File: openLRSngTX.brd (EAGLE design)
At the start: 50 x 40 mm, 33 parts, among them IC1 RFM23BPSMD, J1 AVR_SPI_PRG_6PTH, Q1 MMBT2222, U1 ATMEGA328P, X1 BU-SMA-V, Y1 16MHz

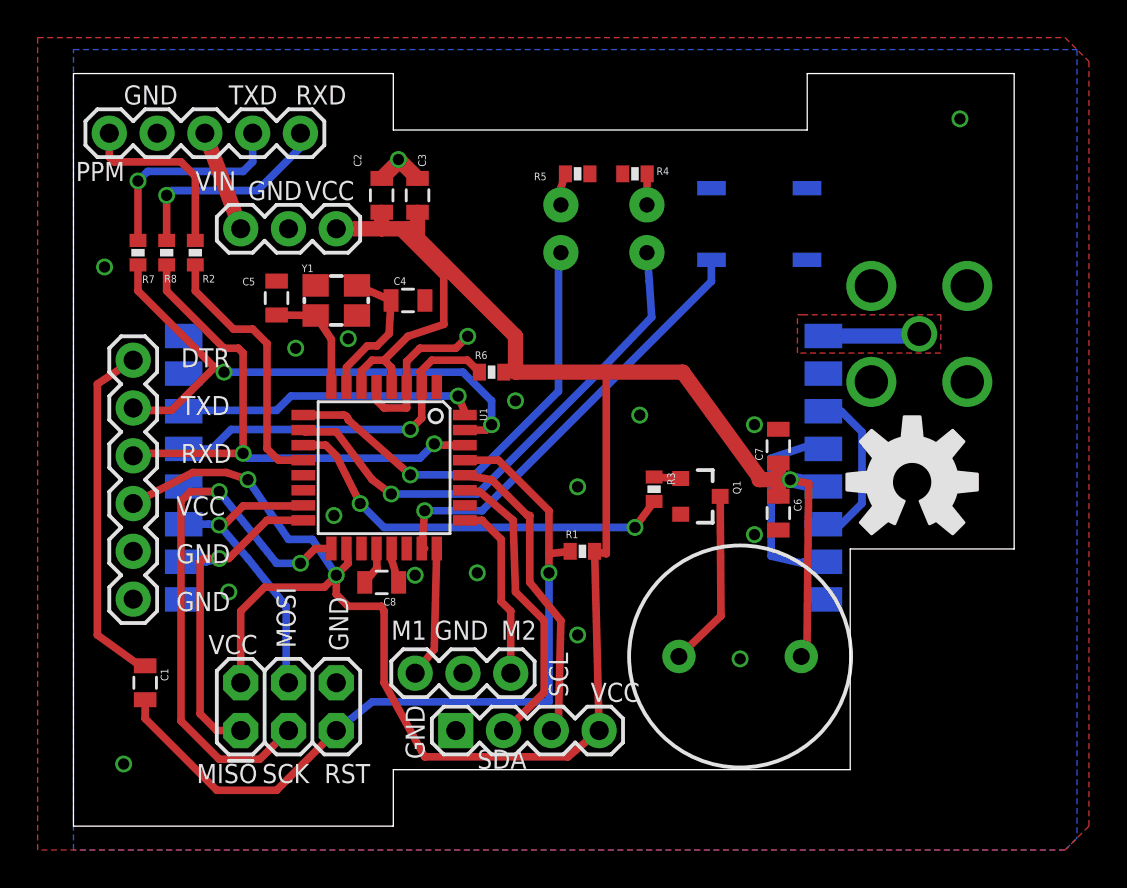
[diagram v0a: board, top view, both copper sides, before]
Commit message: Fix connector towards transmitter (it was wrong way around!). Minor clearance cleanups.
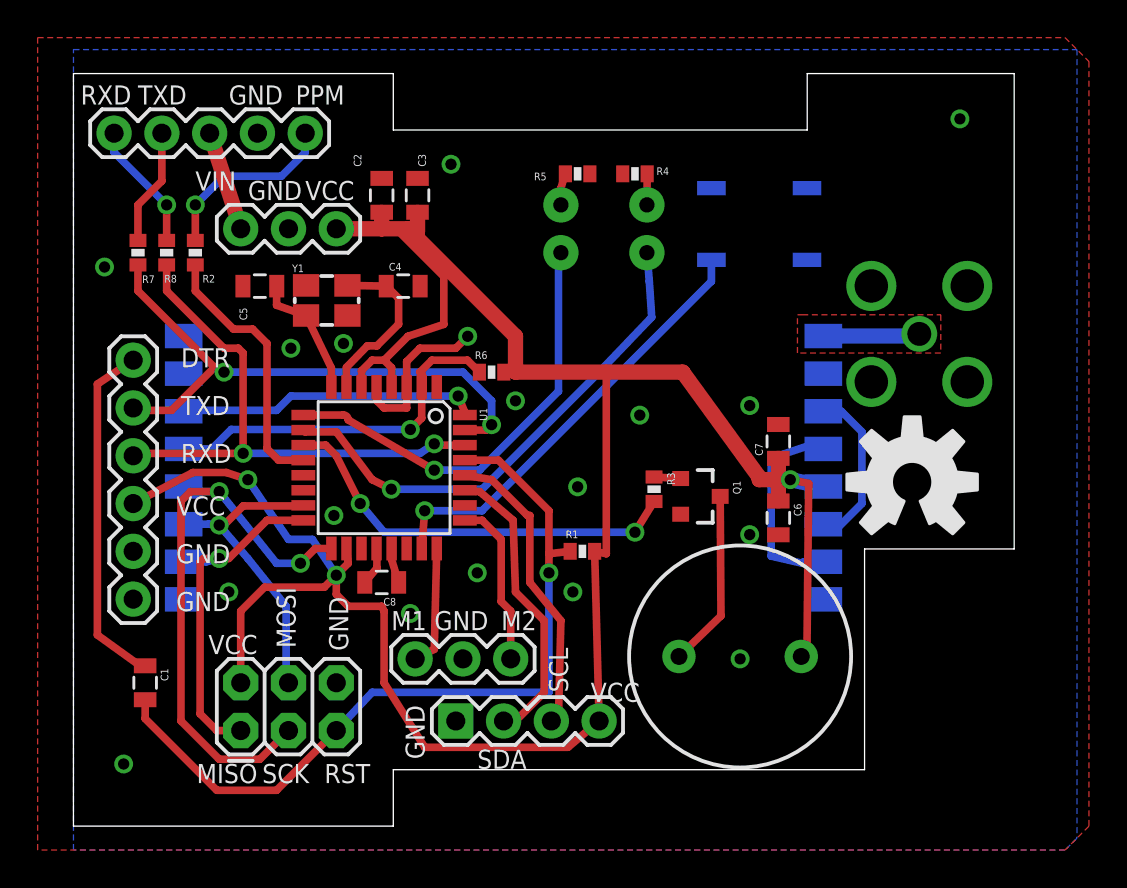
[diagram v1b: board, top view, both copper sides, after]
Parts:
- moved JP1 10.4 mm to (11.7, 36.8), turned to 180 degrees
- moved C5 1.09 mm to (9.27, 28.7), turned to 180 degrees
- moved C4 0.80 mm to (16.9, 28.7)
- moved JP5 0.76 mm to (17.5, 8.89)
- moved Y1 0.51 mm to (12.8, 27.9)
- moved JP3 0.51 mm to (19.7, 5.59)
- moved C6 0.25 mm to (36.8, 16.4)
- moved C7 0.25 mm to (36.8, 20.4)
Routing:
- net N$17: track 11.2 -> 6.23 mm, vias 1 -> 0
- net N$20: track 11.3 -> 6.86 mm
- net GND: track 13.4 -> 10.6 mm
- net N$11: track 7.81 -> 9.14 mm
- net N$19: track 9.67 -> 8.91 mm
- net N$3: track 9.68 -> 9.91 mm, vias 0 -> 1
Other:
- outline, holes or cut-outs redrawn

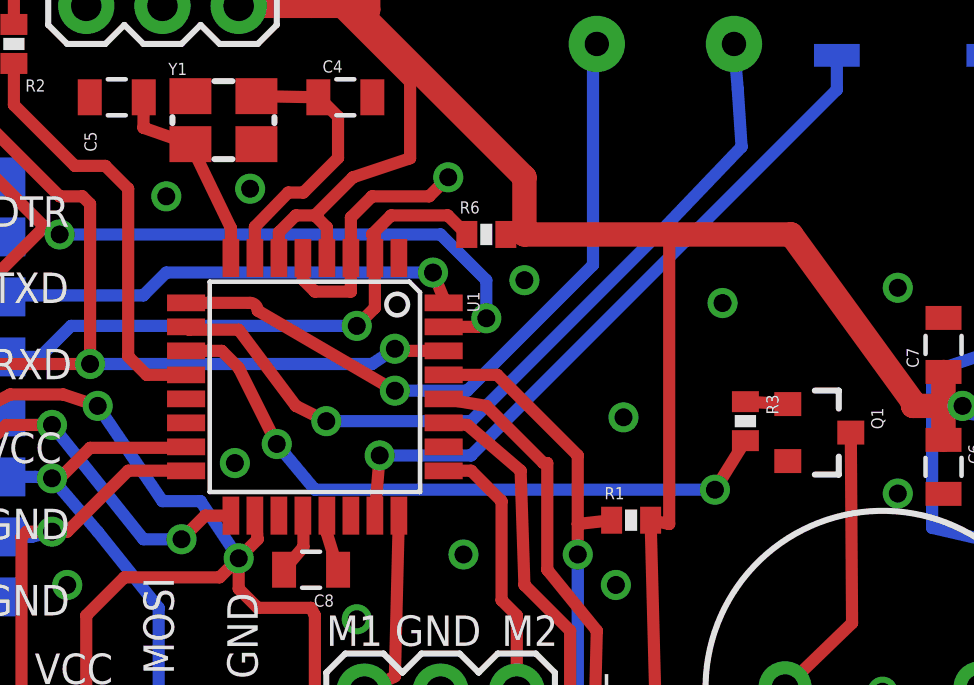
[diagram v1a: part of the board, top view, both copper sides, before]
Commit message: Fix buzzer to correct pin.
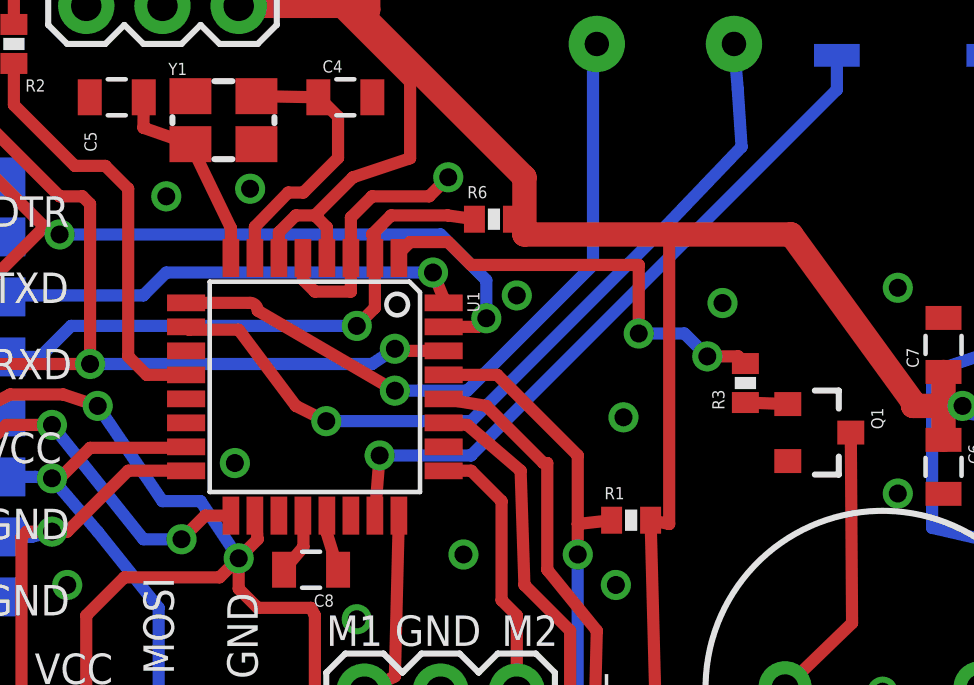
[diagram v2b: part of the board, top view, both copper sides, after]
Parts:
- moved R3 1.27 mm to (30.2, 19.2), turned to 90 degrees
- moved R6 0.57 mm to (21.8, 24.6)
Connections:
- net N$4: now also U1.1; no longer U1.11
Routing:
- net N$4: track 22.1 -> 14.9 mm
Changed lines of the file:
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@@
 <attribute name="VALUE" x="6.2865" y="28.321" size="0.4064" layer="27"/>
 </element>
-<element name="R3" library="SparkFun-Resistors" package="0402-RES" value="1k" x="30.226" y="17.907" rot="R270"/>
+<element name="R3" library="SparkFun-Resistors" package="0402-RES" value="1k" x="30.226" y="19.177" rot="R90"/>
 <element name="R4" library="SparkFun-Resistors" package="0402-RES" value="220R" x="29.21" y="34.671" smashed="yes">
 <attribute name="NAME" x="30.353" y="34.6075" size="0.4064" layer="25"/>
@@
 <element name="C6" library="SparkFun-Capacitors" package="0805" value="1uF" x="36.83" y="16.383" rot="R270"/>
 <element name="C7" library="SparkFun-Capacitors" package="0805" value="100n" x="36.83" y="20.447" rot="R90"/>
-<element name="R6" library="SparkFun-Resistors" package="0402-RES" value="1k" x="21.59" y="24.13"/>
+<element name="R6" library="SparkFun-Resistors" package="0402-RES" value="1k" x="21.844" y="24.638"/>
 <element name="C8" library="SparkFun-Capacitors" package="0805" value="100n" x="15.748" y="12.954" rot="R180"/>
 <element name="S1" library="SparkFun-Electromechanical" package="TACTILE_SWITCH_SMD" value="SWITCH-MOMENTARY-2SMD" x="35.814" y="32.004" smashed="yes" rot="MR180">
@@
 <via x="26.162" y="18.034" extent="1-16" drill="0.6"/>
 <via x="1.016" y="29.718" extent="1-16" drill="0.6"/>
-<via x="22.86" y="22.606" extent="1-16" drill="0.6"/>
+<via x="22.606" y="22.098" extent="1-16" drill="0.6"/>
 <via x="29.464" y="21.844" extent="1-16" drill="0.6"/>
 <via x="20.828" y="13.462" extent="1-16" drill="0.6"/>
@@
 <contactref element="R6" pad="2"/>
 <wire x1="15.748" y1="31.75" x2="13.335" y2="31.75" width="0.8128" layer="1"/>
-<wire x1="22.24" y1="24.13" x2="22.86" y2="24.13" width="0.4064" layer="1"/>
+<wire x1="22.494" y1="24.638" x2="22.86" y2="24.13" width="0.4064" layer="1"/>
 <wire x1="15.748" y1="32.628" x2="15.748" y2="31.75" width="0.8128" layer="1"/>
 <wire x1="17.653" y1="32.628" x2="17.653" y2="31.623" width="0.8128" layer="1"/>
@@
 <wire x1="11.684" y1="35.814" x2="11.684" y2="36.83" width="0.4064" layer="16"/>
 </signal>
-<signal name="N$4">
-<contactref element="R3" pad="2"/>
-<contactref element="U1" pad="11"/>
-<wire x1="11.5824" y1="20.25" x2="12.77" y2="20.25" width="0.4064" layer="1"/>
-<wire x1="12.77" y1="20.25" x2="13.335" y2="19.685" width="0.4064" layer="1"/>
-<wire x1="13.335" y1="19.685" x2="14.605" y2="17.145" width="0.4064" layer="1"/>
-<via x="14.605" y="17.145" extent="1-16" drill="0.6"/>
-<wire x1="14.605" y1="17.145" x2="15.875" y2="15.621" width="0.4064" layer="16"/>
-<wire x1="15.875" y1="15.621" x2="29.21" y2="15.621" width="0.4064" layer="16"/>
-<via x="29.21" y="15.621" extent="1-16" drill="0.6"/>
-<wire x1="29.21" y1="15.621" x2="30.226" y2="17.257" width="0.4064" layer="1"/>
-</signal>
 <signal name="N$5">
 <contactref element="R3" pad="1"/>
 <contactref element="Q1" pad="1"/>
-<wire x1="31.639" y1="18.476" x2="30.226" y2="18.557" width="0.4064" layer="1"/>
+<wire x1="31.639" y1="18.476" x2="30.226" y2="18.527" width="0.4064" layer="1"/>
 </signal>
 <signal name="N$6">
@@
 <wire x1="6.715" y1="20.05" x2="7.747" y2="21.082" width="0.4064" layer="16"/>
 <contactref element="R6" pad="1"/>
-<wire x1="20.94" y1="24.13" x2="20.305" y2="24.765" width="0.4064" layer="1"/>
+<wire x1="21.194" y1="24.638" x2="20.305" y2="24.765" width="0.4064" layer="1"/>
 <wire x1="20.305" y1="24.765" x2="18.415" y2="24.765" width="0.4064" layer="1"/>
 <wire x1="18.415" y1="24.765" x2="17.78" y2="24.13" width="0.4064" layer="1"/>
@@
 <wire x1="1.524" y1="35.814" x2="1.524" y2="36.83" width="0.4064" layer="16"/>
 </signal>
+<signal name="N$4">
+<contactref element="R3" pad="2"/>
+<contactref element="U1" pad="1"/>
+<wire x1="18.675" y1="23.3426" x2="18.675" y2="23.501" width="0.4064" layer="1"/>
+<wire x1="18.675" y1="23.501" x2="19.05" y2="23.876" width="0.4064" layer="1"/>
+<wire x1="19.05" y1="23.876" x2="20.32" y2="23.876" width="0.4064" layer="1"/>
+<wire x1="20.32" y1="23.876" x2="21.082" y2="23.114" width="0.4064" layer="1"/>
+<wire x1="21.082" y1="23.114" x2="26.67" y2="23.114" width="0.4064" layer="1"/>
+<wire x1="26.67" y1="23.114" x2="26.67" y2="20.828" width="0.4064" layer="1"/>
+<via x="26.67" y="20.828" extent="1-16" drill="0.6"/>
+<wire x1="26.67" y1="20.828" x2="28.194" y2="20.828" width="0.4064" layer="16"/>
+<wire x1="28.194" y1="20.828" x2="28.956" y2="20.066" width="0.4064" layer="16"/>
+<via x="28.956" y="20.066" extent="1-16" drill="0.6"/>
+<wire x1="28.956" y1="20.066" x2="29.987" y2="20.066" width="0.4064" layer="1"/>
+<wire x1="29.987" y1="20.066" x2="30.226" y2="19.827" width="0.4064" layer="1"/>
+</signal>
 </signals>

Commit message: cleanups
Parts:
- R1, R2, R3, R4, R5, R6, R7, R8: device SparkFun-Resistors:0402-RES -> SparkFun-Resistors:0805
- moved R3 1.45 mm to (31.4, 20.1), turned to 180 degrees
- moved R6 1.02 mm to (22.9, 24.6)
- moved IC1 0.57 mm to (22.0, 19.6)
- moved X1 0.51 mm to (44.3, 26.7)
- moved R4 0.25 mm to (29.2, 34.9)
- moved R5 0.25 mm to (26.2, 34.9)
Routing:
- net SDA: track 16.3 -> 15.3 mm
- net RF_CS: track 19.5 -> 20.3 mm
- net SCK: track 31.2 -> 31.8 mm

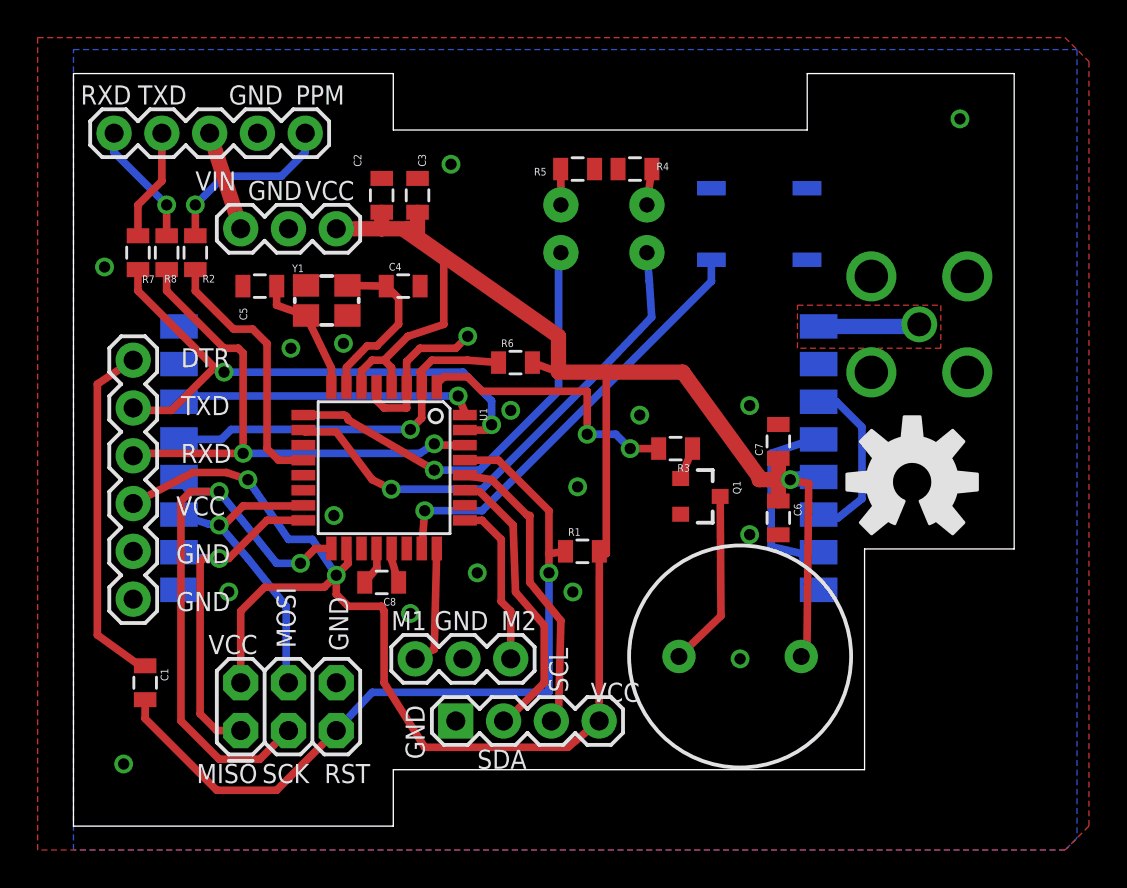
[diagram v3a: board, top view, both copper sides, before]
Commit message: Updated design rules, now vias are masked.
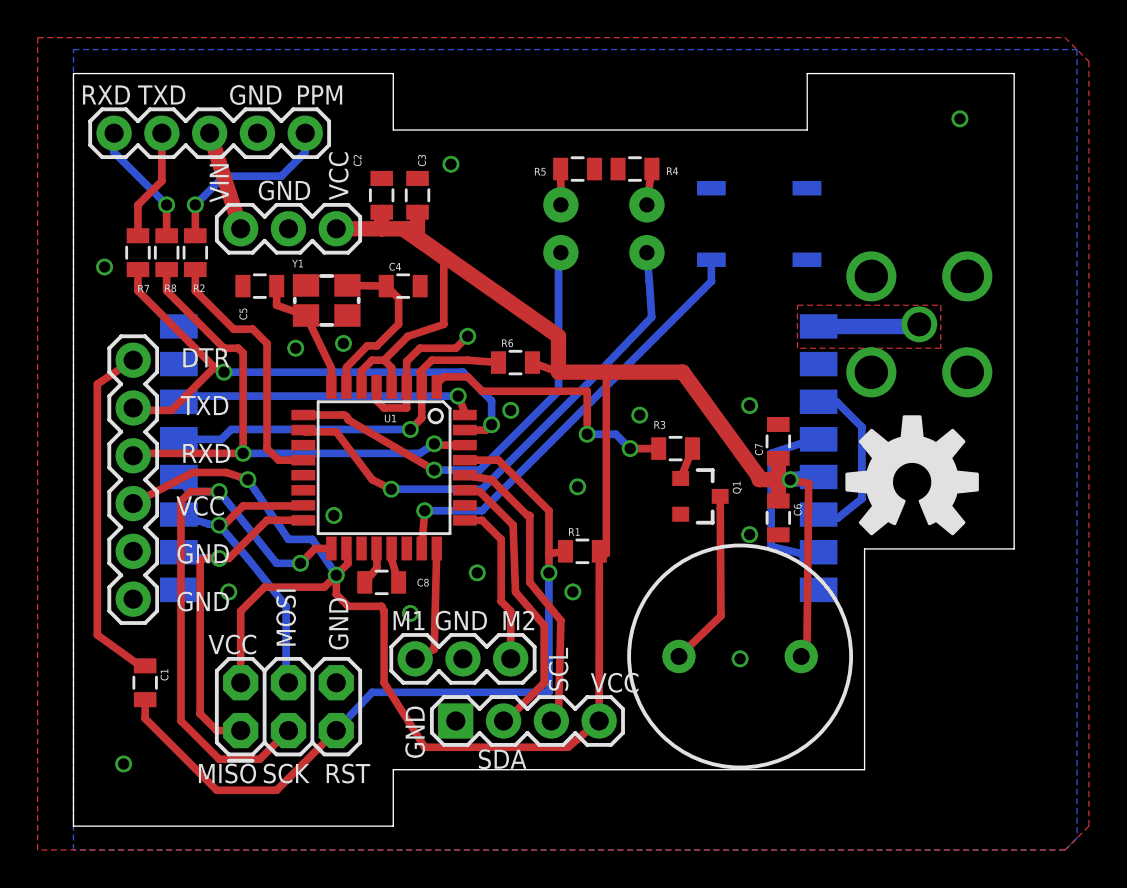
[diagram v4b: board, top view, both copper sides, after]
